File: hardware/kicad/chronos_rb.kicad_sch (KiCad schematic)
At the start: 0 parts

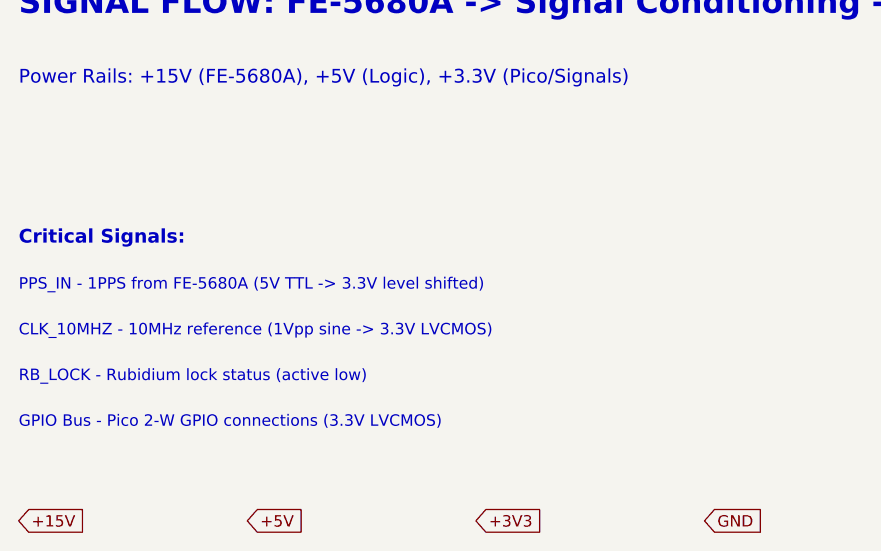
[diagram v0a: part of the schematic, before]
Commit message: Fix 1PPS documentation: FE-5680A DB-9 has no native 1PPS output
Most FE-5680A units (including the DB-9 +15V/+5V version) do NOT have a native
1PPS output - only 10MHz. Updated all documentation and code comments to reflect
that 1PPS must be derived from the 10MHz reference using a divider circuit, or
sourced from an external GPS/GNSS receiver.

Changes:
- Updated firmware comments (pps_capture.c, chronos_rb.h, cli.c)
- Fixed FE-5680A pinout in all documentation (DB-9: Pin 1=+15V, Pin 2=GND,
  Pin 3=Lock, Pin 4=+5V, Pin 5=GND, Pin 7=10MHz)
- Updated signal flow diagrams and block diagrams
- Changed 1PPS level shifter references to indicate it's for external sources
- Fixed KiCad schematic descriptions
- Updated SVG wiring diagrams with correct pinout and signal sources

🤖 Generated with [Claude Code](https://claude.com/claude-code)

Co-Authored-By: Claude Opus 4.5 <noreply@anthropic.com>
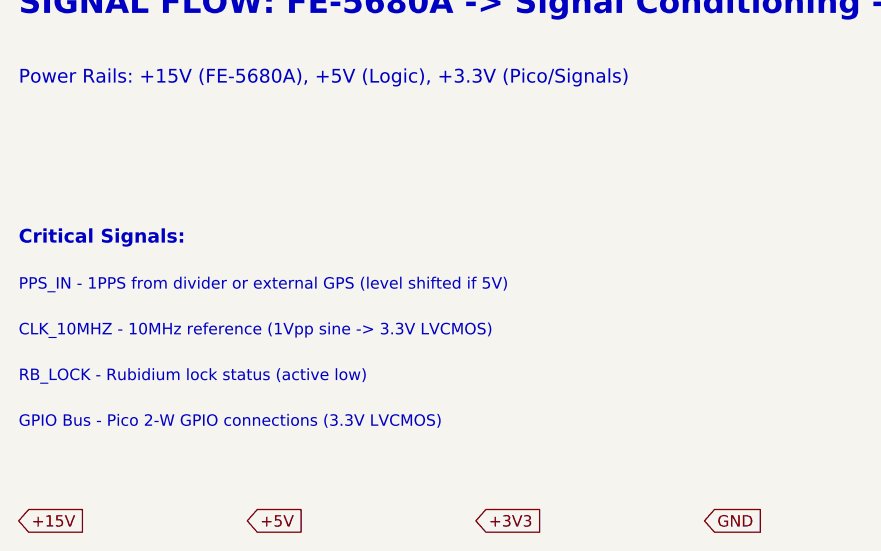
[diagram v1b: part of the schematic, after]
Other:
- note added: "PPS_IN - 1PPS from divider or external GPS (level shifted if 5V)"
- note removed: "PPS_IN - 1PPS from FE-5680A (5V TTL -> 3.3V level shifted)"
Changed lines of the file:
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@@
 		)
 	)
-	(text "PPS_IN - 1PPS from FE-5680A (5V TTL -> 3.3V level shifted)"
+	(text "PPS_IN - 1PPS from divider or external GPS (level shifted if 5V)"
 		(exclude_from_sim no)
 		(at 25.4 106.68 0)
